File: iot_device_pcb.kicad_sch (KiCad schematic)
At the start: 25 parts, among them J1 B2B-PH-K-S_LF__SN_, J2 USB_C_Receptacle_USB2.0_16P, U1 AMS1117-3.3, U2 MCP73871

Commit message: chore(sch): update footprint for single-pin connector
Replace the existing JST B2B-PH footprint with a JST ACH BM01B
vertical 1x01 connector to match updated hardware specifications.
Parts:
- J1: footprint FootPrints:JST_B2B-PH-K-S_LF__SN_ -> Connector_JST:JST_ACH_BM01B-ACHSS-A-GAN-ETF_1x01-1MP_P1.20mm_Vertical
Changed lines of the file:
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@@
 			)
 		)
-		(property "Footprint" "FootPrints:JST_B2B-PH-K-S_LF__SN_"
+		(property "Footprint" "Connector_JST:JST_ACH_BM01B-ACHSS-A-GAN-ETF_1x01-1MP_P1.20mm_Vertical"
 			(at 29.21 135.89 0)
 			(effects

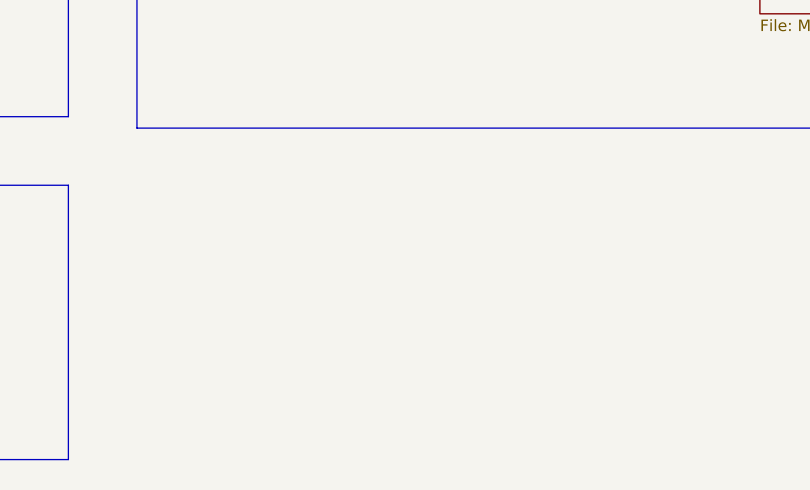
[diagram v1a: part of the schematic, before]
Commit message: feat(sch): add mounting holes to schematic
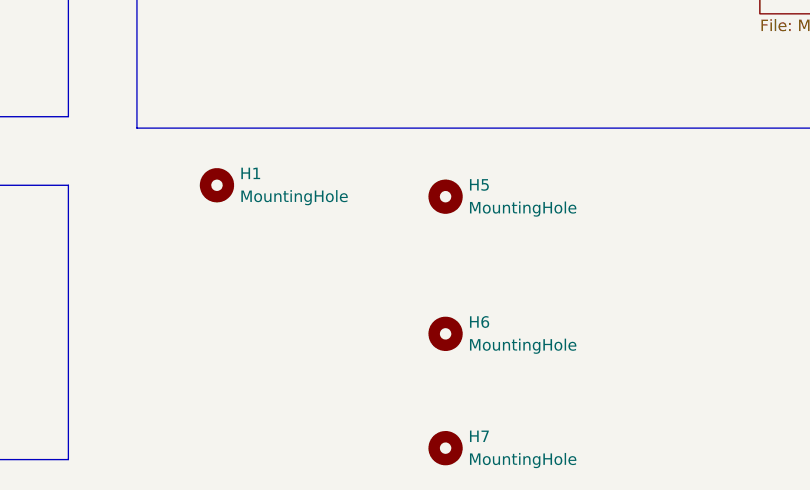
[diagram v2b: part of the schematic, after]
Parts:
- added H1, H5, H6, H7: MountingHole, MountingHole:MountingHole_2.5mm_Pad_Via, symbol Mechanical:MountingHole
